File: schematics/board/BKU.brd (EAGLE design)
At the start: 94 x 94 mm, 60 parts

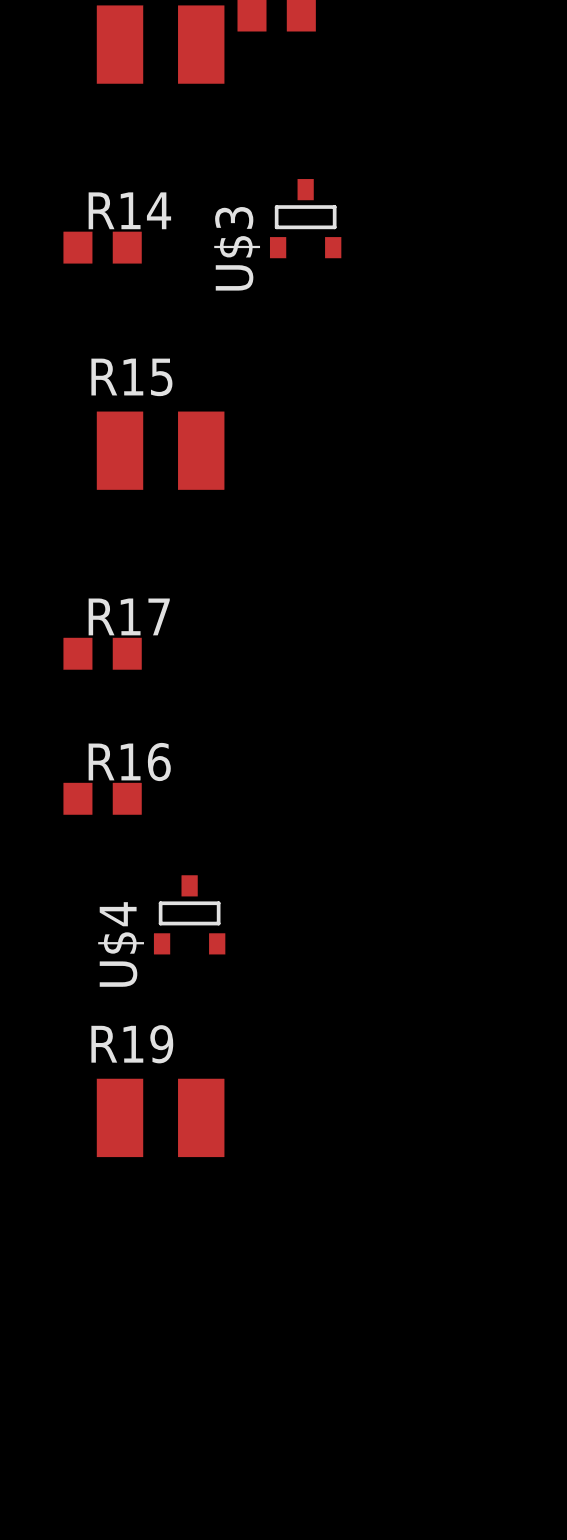
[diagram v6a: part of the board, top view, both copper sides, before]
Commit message: На платах БСК устройства по умолчанию подтянуты к питанию
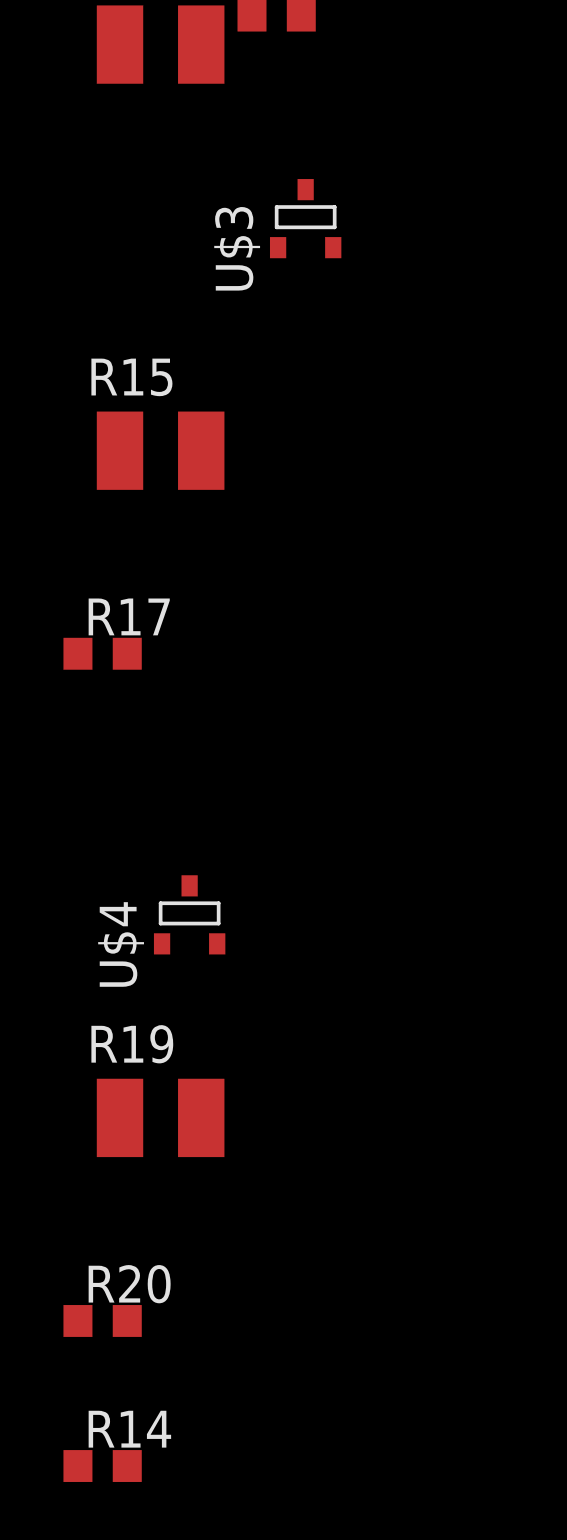
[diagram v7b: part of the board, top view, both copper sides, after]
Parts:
- removed R16: 1M, resistor:R0603
- added R20: 1M, resistor:R0603
- moved R14 42.0 mm to (-30.0, -157.0)
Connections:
- net 3V3: now also R14.1, R20.1
- net GND: no longer R14.2, R16.2
- net N$11: now also R20.2; no longer R14.1
- net N$6: now also R14.2; no longer R16.1
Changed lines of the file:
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@@
 <attribute name="NAME" x="-24.8288" y="-116.6162" size="1.27" layer="25" ratio="10" rot="R90"/>
-</element>
-<element name="R14" library="resistor" package="R0603" package3d_urn="urn:adsk.eagle:package:23555/3" value="1M" x="-30" y="-115" smashed="yes">
-<attribute name="NAME" x="-30.635" y="-114.365" size="1.27" layer="25"/>
-<attribute name="VALUE" x="-30.635" y="-116.905" size="1.27" layer="27"/>
 </element>
 <element name="R31" library="resistor" package="R0603" package3d_urn="urn:adsk.eagle:package:23555/3" value="100R" x="-24" y="-107" smashed="yes">
@@
 <attribute name="NAME" x="-28.8288" y="-140.6162" size="1.27" layer="25" ratio="10" rot="R90"/>
 </element>
-<element name="R16" library="resistor" package="R0603" package3d_urn="urn:adsk.eagle:package:23555/3" value="1M" x="-30" y="-134" smashed="yes">
-<attribute name="NAME" x="-30.635" y="-133.365" size="1.27" layer="25"/>
-<attribute name="VALUE" x="-30.635" y="-135.905" size="1.27" layer="27"/>
-</element>
 <element name="R17" library="resistor" package="R0603" package3d_urn="urn:adsk.eagle:package:23555/3" value="100R" x="-30" y="-129" smashed="yes">
 <attribute name="NAME" x="-30.635" y="-128.365" size="1.27" layer="25"/>
@@
 <attribute name="SPICEPREFIX" value="R" x="-28" y="-145" size="1.778" layer="27" display="off"/>
 <attribute name="VALUE" x="-30.54" y="-148.175" size="1.27" layer="27"/>
+</element>
+<element name="R20" library="resistor" package="R0603" package3d_urn="urn:adsk.eagle:package:23555/3" value="1M" x="-30" y="-152" smashed="yes">
+<attribute name="NAME" x="-30.635" y="-151.365" size="1.27" layer="25"/>
+<attribute name="VALUE" x="-30.635" y="-153.905" size="1.27" layer="27"/>
+</element>
+<element name="R14" library="resistor" package="R0603" package3d_urn="urn:adsk.eagle:package:23555/3" value="1M" x="-30" y="-157" smashed="yes">
+<attribute name="NAME" x="-30.635" y="-156.365" size="1.27" layer="25"/>
+<attribute name="VALUE" x="-30.635" y="-158.905" size="1.27" layer="27"/>
 </element>
 </elements>
@@
 <contactref element="R7" pad="1"/>
 <contactref element="U$3" pad="2"/>
-<contactref element="R14" pad="2"/>
 <contactref element="R33" pad="1"/>
 <contactref element="U$4" pad="2"/>
-<contactref element="R16" pad="2"/>
 <contactref element="R19" pad="1"/>
 <contactref element="U$1" pad="2"/>
@@
 <contactref element="U$1" pad="20"/>
 <wire x1="-26.05" y1="-139" x2="-29.4" y2="-145" width="0" layer="19" extent="1-1"/>
-<wire x1="-29.15" y1="-134" x2="-26.05" y2="-139" width="0" layer="19" extent="1-1"/>
-<wire x1="-29.15" y1="-115" x2="-29.15" y2="-134" width="0" layer="19" extent="1-1"/>
-<wire x1="-29.4" y1="-108" x2="-29.15" y2="-115" width="0" layer="19" extent="1-1"/>
-<wire x1="-22.05" y1="-115" x2="-29.15" y2="-115" width="0" layer="19" extent="1-1"/>
+<wire x1="-22.05" y1="-115" x2="-26.05" y2="-139" width="0" layer="19" extent="1-1"/>
+<wire x1="-29.4" y1="-108" x2="-22.05" y2="-115" width="0" layer="19" extent="1-1"/>
 <wire x1="-26.85" y1="-99" x2="-29.4" y2="-108" width="0" layer="19" extent="1-1"/>
 <wire x1="-29.9" y1="-88.275" x2="-26.85" y2="-99" width="0" layer="19" extent="1-1"/>
@@
 <contactref element="U$21" pad="P$3"/>
 <contactref element="LED-G" pad="A"/>
-<wire x1="85.35" y1="73.3" x2="103.1" y2="54.08" width="0" layer="19" extent="1-1"/>
-<wire x1="81.45" y1="73.3" x2="85.35" y2="73.3" width="0" layer="19" extent="1-1"/>
-<wire x1="85.25" y1="23" x2="103.1" y2="54.08" width="0" layer="19" extent="1-1"/>
-<wire x1="81.35" y1="23" x2="85.25" y2="23" width="0" layer="19" extent="1-1"/>
-<wire x1="76.75" y1="12.7" x2="81.35" y2="23" width="0" layer="19" extent="1-1"/>
+<contactref element="R20" pad="1"/>
+<contactref element="R14" pad="1"/>
+<wire x1="-30.85" y1="-152" x2="-30.85" y2="-157" width="0" layer="19" extent="1-1"/>
+<wire x1="-29" y1="-102.75" x2="-30.85" y2="-152" width="0" layer="19" extent="1-1"/>
+<wire x1="-26" y1="-89.35" x2="-29" y2="-102.75" width="0" layer="19" extent="1-1"/>
+<wire x1="-24.1" y1="-87.625" x2="-26" y2="-89.35" width="0" layer="19" extent="1-1"/>
+<wire x1="-24.1" y1="-83.725" x2="-24.1" y2="-87.625" width="0" layer="19" extent="1-1"/>
+<wire x1="-29.15" y1="-54" x2="-24.1" y2="-83.725" width="0" layer="19" extent="1-1"/>
+<wire x1="16.72" y1="9.8" x2="-29.15" y2="-54" width="0" layer="19" extent="1-1"/>
+<wire x1="18.28" y1="9.84" x2="16.72" y2="9.8" width="0" layer="19" extent="1-1"/>
+<wire x1="16.72" y1="11.94" x2="16.72" y2="9.8" width="0" layer="19" extent="1-1"/>
+<wire x1="37.65" y1="-4.1" x2="18.28" y2="9.84" width="0" layer="19" extent="1-1"/>
+<wire x1="45.25" y1="13" x2="37.65" y2="-4.1" width="0" layer="19" extent="1-1"/>
+<wire x1="46.65" y1="13" x2="45.25" y2="13" width="0" layer="19" extent="1-1"/>
+<wire x1="46.65" y1="15.1" x2="46.65" y2="13" width="0" layer="19" extent="1-1"/>
+<wire x1="45.25" y1="15.1" x2="46.65" y2="15.1" width="0" layer="19" extent="1-1"/>
+<wire x1="46.65" y1="17.2" x2="46.65" y2="15.1" width="0" layer="19" extent="1-1"/>
+<wire x1="45.25" y1="17.2" x2="46.65" y2="17.2" width="0" layer="19" extent="1-1"/>
+<wire x1="58.9" y1="16.77" x2="46.65" y2="17.2" width="0" layer="19" extent="1-1"/>
+<wire x1="76.75" y1="12.7" x2="58.9" y2="16.77" width="0" layer="19" extent="1-1"/>
 <wire x1="76.75" y1="8.8" x2="76.75" y2="12.7" width="0" layer="19" extent="1-1"/>
-<wire x1="58.9" y1="16.77" x2="76.75" y2="12.7" width="0" layer="19" extent="1-1"/>
-<wire x1="46.65" y1="17.2" x2="58.9" y2="16.77" width="0" layer="19" extent="1-1"/>
-<wire x1="45.25" y1="17.2" x2="46.65" y2="17.2" width="0" layer="19" extent="1-1"/>
-<wire x1="46.65" y1="15.1" x2="46.65" y2="17.2" width="0" layer="19" extent="1-1"/>
-<wire x1="45.25" y1="15.1" x2="46.65" y2="15.1" width="0" layer="19" extent="1-1"/>
-<wire x1="46.65" y1="13" x2="46.65" y2="15.1" width="0" layer="19" extent="1-1"/>
-<wire x1="45.25" y1="13" x2="46.65" y2="13" width="0" layer="19" extent="1-1"/>
-<wire x1="37.65" y1="-4.1" x2="45.25" y2="13" width="0" layer="19" extent="1-1"/>
+<wire x1="81.35" y1="23" x2="76.75" y2="12.7" width="0" layer="19" extent="1-1"/>
+<wire x1="85.25" y1="23" x2="81.35" y2="23" width="0" layer="19" extent="1-1"/>
 <wire x1="27.99" y1="33" x2="45.25" y2="17.2" width="0" layer="19" extent="1-1"/>
 <wire x1="28.65" y1="39.01" x2="27.99" y2="33" width="0" layer="19" extent="1-1"/>
@@
 <wire x1="31.8" y1="40.7" x2="30.46" y2="38.67" width="0" layer="19" extent="1-1"/>
 <wire x1="33.11" y1="38.32" x2="30.46" y2="38.67" width="0" layer="19" extent="1-1"/>
-<wire x1="18.28" y1="9.84" x2="37.65" y2="-4.1" width="0" layer="19" extent="1-1"/>
-<wire x1="16.72" y1="9.8" x2="18.28" y2="9.84" width="0" layer="19" extent="1-1"/>
-<wire x1="16.72" y1="11.94" x2="16.72" y2="9.8" width="0" layer="19" extent="1-1"/>
 <wire x1="-5.1" y1="48.92" x2="28.65" y2="39.01" width="0" layer="19" extent="1-1"/>
+<wire x1="103.1" y1="54.08" x2="85.25" y2="23" width="0" layer="19" extent="1-1"/>
+<wire x1="85.35" y1="73.3" x2="103.1" y2="54.08" width="0" layer="19" extent="1-1"/>
+<wire x1="81.45" y1="73.3" x2="85.35" y2="73.3" width="0" layer="19" extent="1-1"/>
 <wire x1="75.22" y1="-33.27" x2="76.75" y2="8.8" width="0" layer="19" extent="1-1"/>
 <wire x1="75.54" y1="-35.4" x2="75.22" y2="-33.27" width="0" layer="19" extent="1-1"/>
@@
 <wire x1="77.39" y1="-37.15" x2="75.52" y2="-37.47" width="0" layer="19" extent="1-1"/>
 <wire x1="46.24" y1="100.8" x2="81.45" y2="73.3" width="0" layer="19" extent="1-1"/>
-<wire x1="-29.15" y1="-54" x2="16.72" y2="9.8" width="0" layer="19" extent="1-1"/>
-<wire x1="-24.1" y1="-83.725" x2="-29.15" y2="-54" width="0" layer="19" extent="1-1"/>
-<wire x1="-24.1" y1="-87.625" x2="-24.1" y2="-83.725" width="0" layer="19" extent="1-1"/>
-<wire x1="-26" y1="-89.35" x2="-24.1" y2="-87.625" width="0" layer="19" extent="1-1"/>
-<wire x1="-29" y1="-102.75" x2="-26" y2="-89.35" width="0" layer="19" extent="1-1"/>
 </signal>
 <signal name="PL6-KVCC">
@@
 <contactref element="R31" pad="2"/>
 <contactref element="U$3" pad="1"/>
-<contactref element="R14" pad="1"/>
-<wire x1="-23.95" y1="-115" x2="-30.85" y2="-115" width="0" layer="19" extent="1-1"/>
+<contactref element="R20" pad="2"/>
+<wire x1="-23.95" y1="-115" x2="-29.15" y2="-152" width="0" layer="19" extent="1-1"/>
 <wire x1="-23.15" y1="-107" x2="-23.95" y2="-115" width="0" layer="19" extent="1-1"/>
 </signal>
@@
 <contactref element="R17" pad="2"/>
 <contactref element="U$4" pad="1"/>
-<contactref element="R16" pad="1"/>
-<wire x1="-30.85" y1="-134" x2="-27.95" y2="-139" width="0" layer="19" extent="1-1"/>
-<wire x1="-29.15" y1="-129" x2="-30.85" y2="-134" width="0" layer="19" extent="1-1"/>
+<contactref element="R14" pad="2"/>
+<wire x1="-27.95" y1="-139" x2="-29.15" y2="-157" width="0" layer="19" extent="1-1"/>
+<wire x1="-29.15" y1="-129" x2="-27.95" y2="-139" width="0" layer="19" extent="1-1"/>
 </signal>
 <signal name="RADIO">
